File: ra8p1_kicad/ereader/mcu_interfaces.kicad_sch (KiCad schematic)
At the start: 3 parts, among them U1 R7KA8P1KFLCAC#UC0

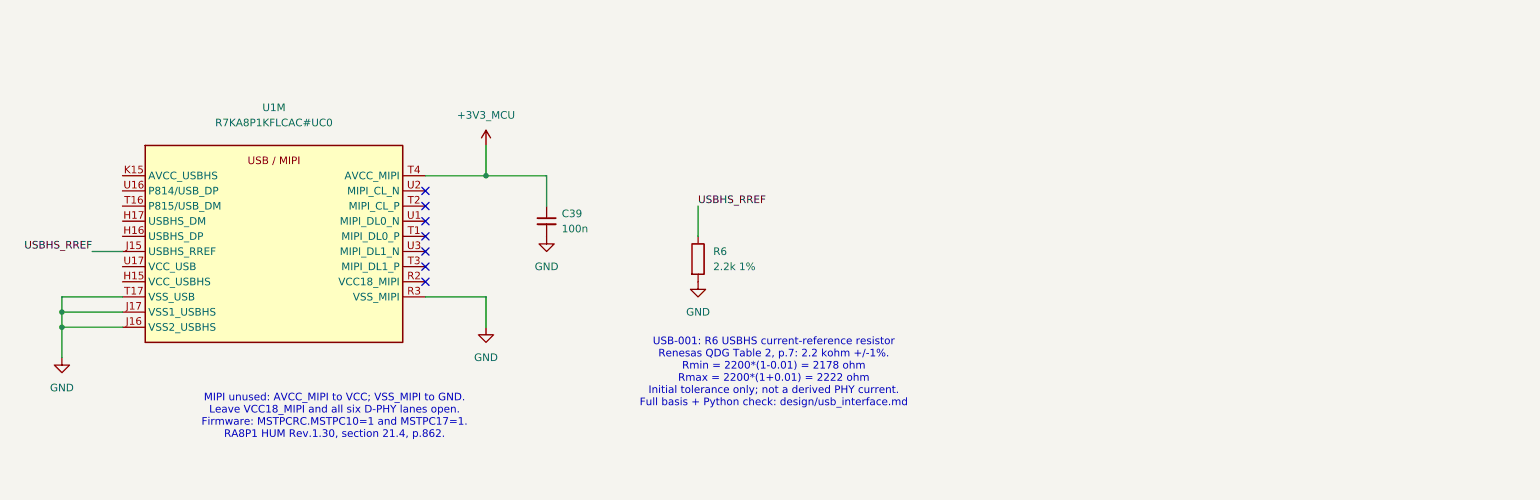
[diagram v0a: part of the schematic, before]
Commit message: feat(hardware): wire USB full-speed supply bypass
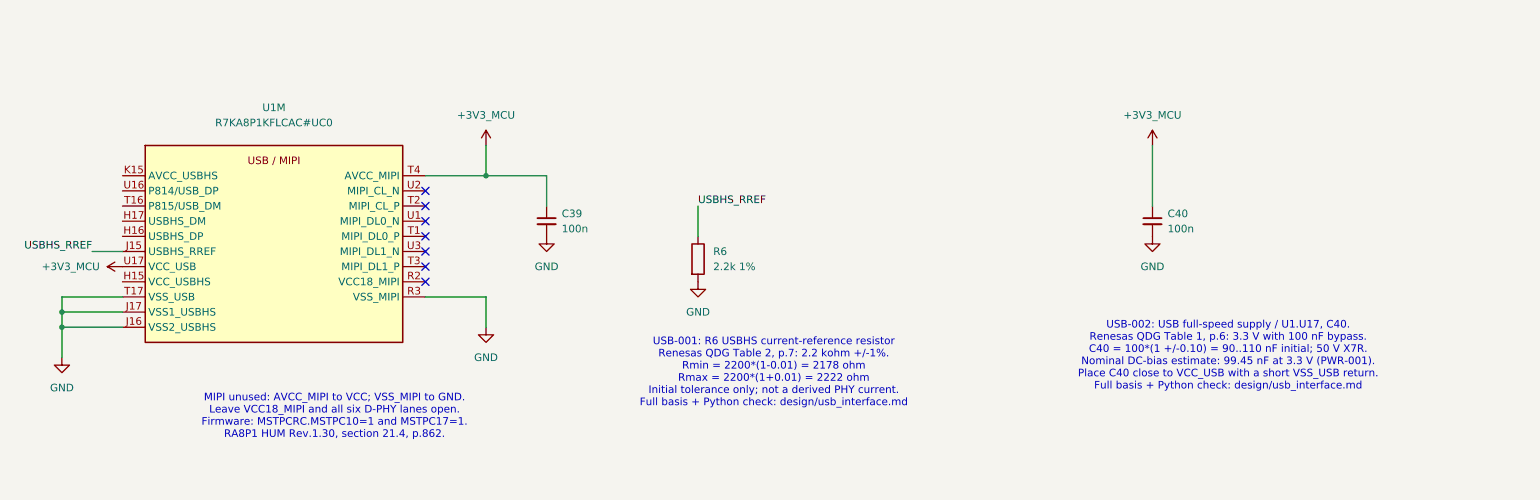
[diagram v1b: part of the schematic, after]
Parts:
- added C40: 100n, symbol Device:C_Small
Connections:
- net +3V3_MCU: now also U1.U17 (VCC_USB), C40.1
- net GND: now also C40.2
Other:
- note added: "USB-002: USB full-speed supply / U1.U17, C40. Renesas QDG Table 1, p.6: 3.3 V with 100 nF bypass. C40 = 100*(1 +/-0.10) = 90..110 nF initial; 50 V X7R. Nominal DC-bias estimate: 99.45 nF at 3.3 V (PWR-001). Place C40 close to VCC_USB with a short VSS_USB return. Full basis + Python check: design/usb_interface.md"

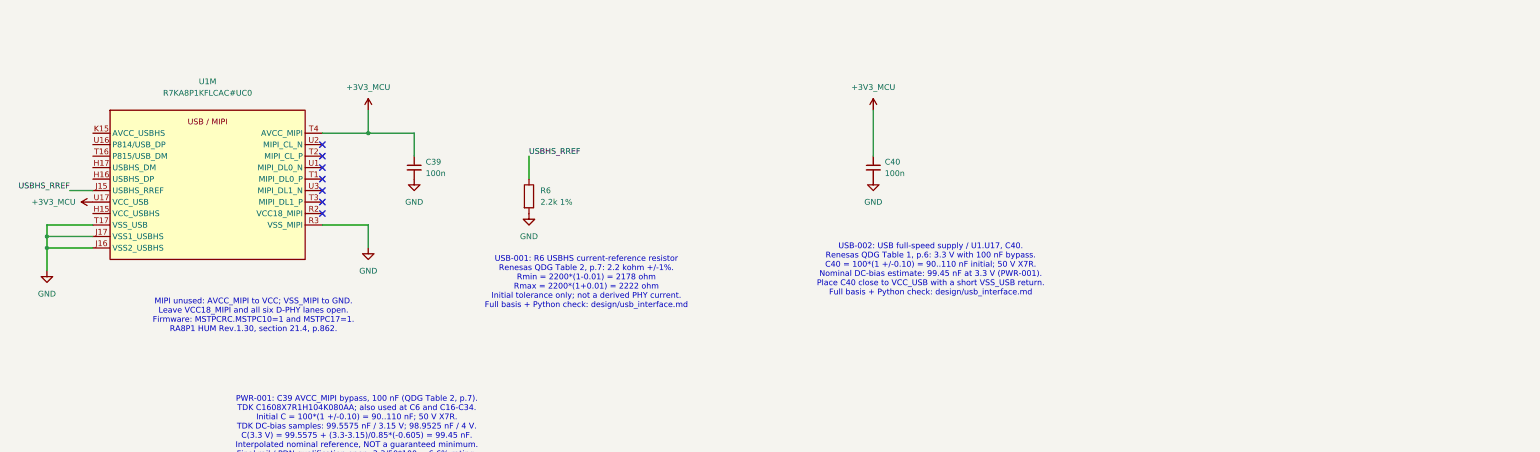
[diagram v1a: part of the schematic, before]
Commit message: feat(hardware): wire USB high-speed supply bypass and bulk
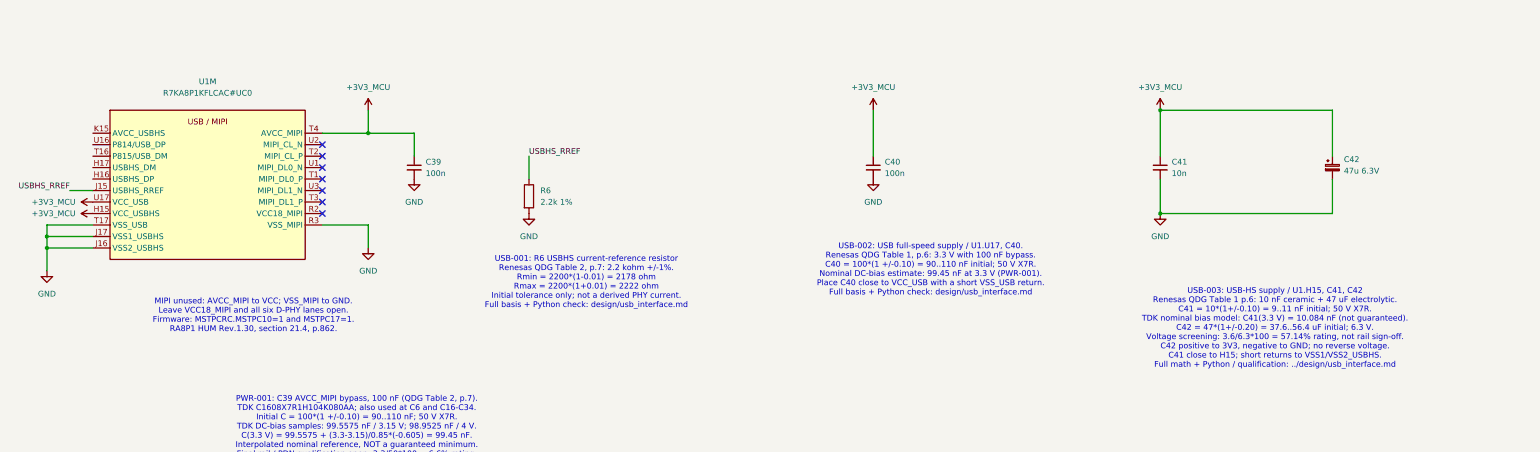
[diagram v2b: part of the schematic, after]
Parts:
- added C41: 10n, symbol Device:C_Small
- added C42: 47u 6.3V, symbol Device:C_Polarized_Small
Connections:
- net +3V3_MCU: now also U1.H15 (VCC_USBHS), C41.1, C42.1
- net GND: now also C41.2, C42.2
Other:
- note added: "USB-003: USB-HS supply / U1.H15, C41, C42 Renesas QDG Table 1 p.6: 10 nF ceramic + 47 uF electrolytic. C41 = 10*(1+/-0.10) = 9..11 nF initial; 50 V X7R. TDK nominal bias model: C41(3.3 V) = 10.084 nF (not guaranteed). C42 = 47*(1+/-0.20) = 37.6..56.4 uF initial; 6.3 V. Voltage screening: 3.6/6.3*100 = 57.14% rating, not rail sign-off. C42 positive to 3V3, negative to GND; no reverse voltage. C41 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"

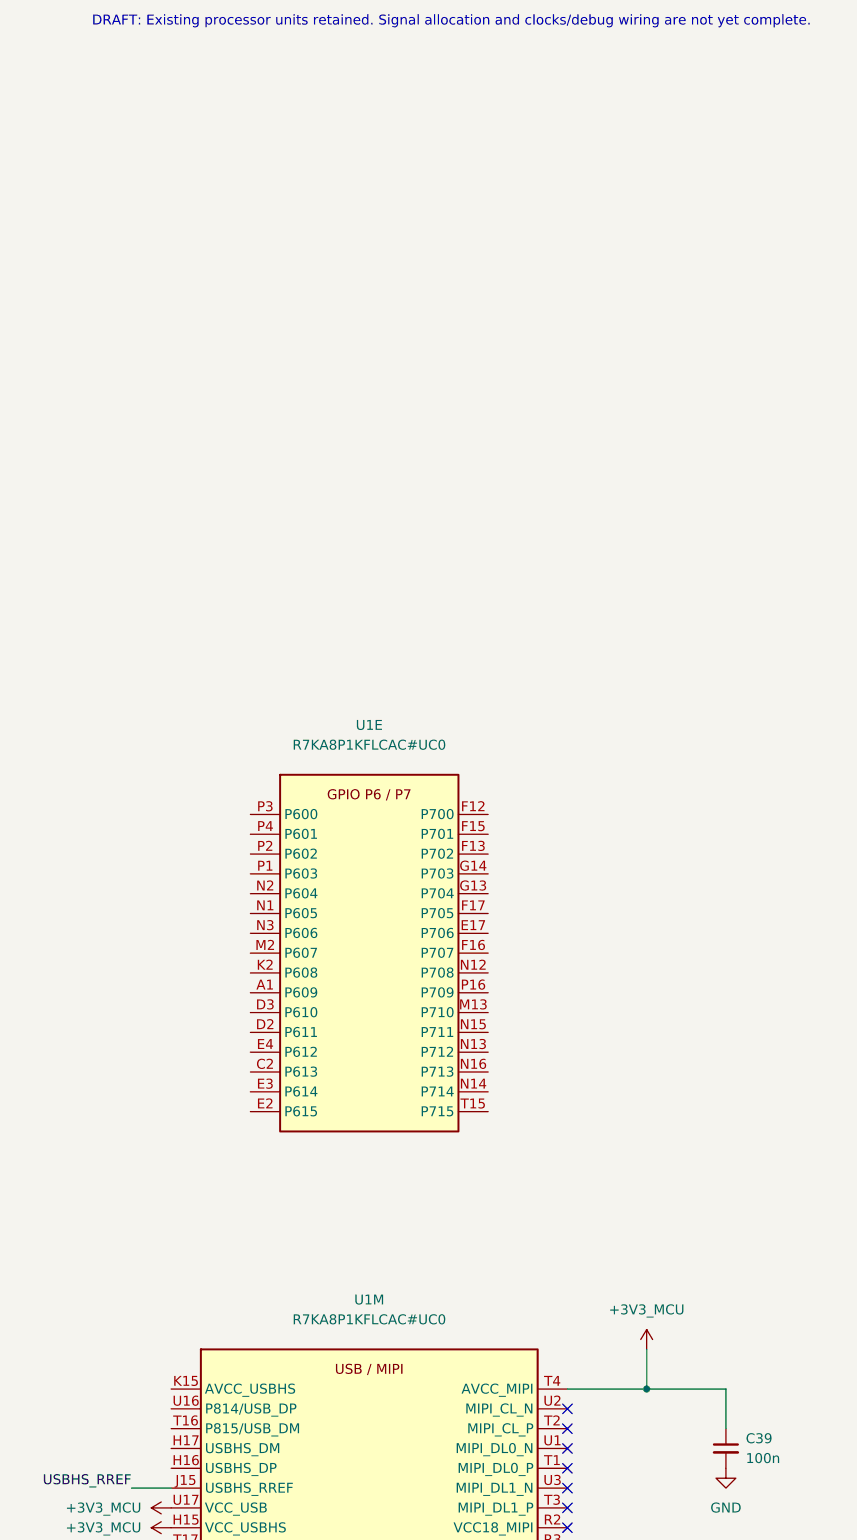
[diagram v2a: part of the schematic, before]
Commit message: feat(hardware): add USB high-speed analog supply filter
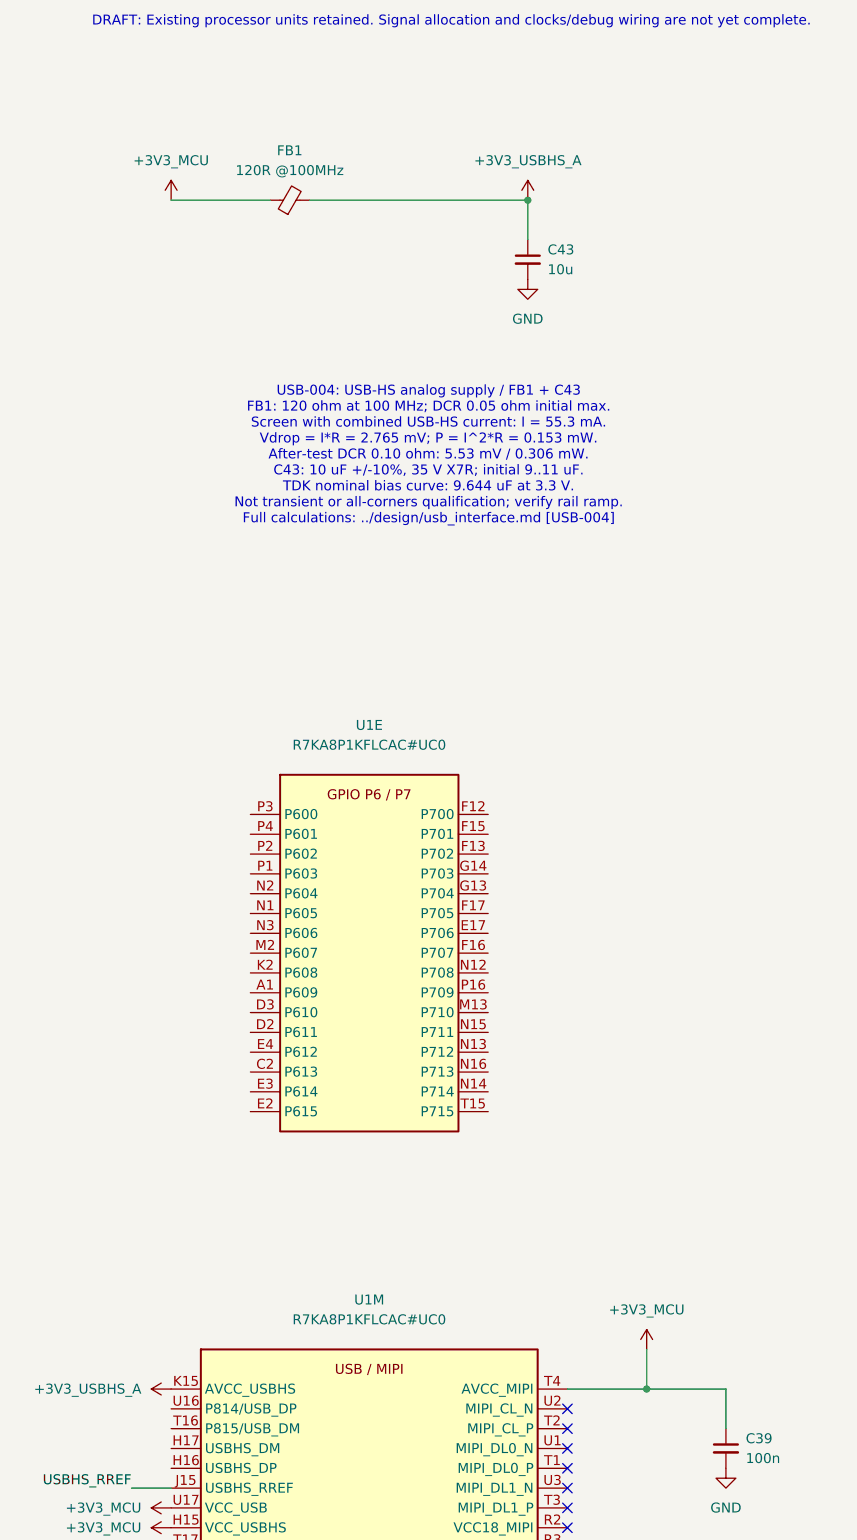
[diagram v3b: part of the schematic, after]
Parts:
- added C43: 10u, symbol Device:C_Small
- added FB1: 120R @100MHz, symbol Device:FerriteBead_Small
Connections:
- net +3V3_MCU: now also FB1.1
- net GND: now also C43.2
- net +3V3_USBHS_A: now reaches U1.K15 (AVCC_USBHS)
- net +3V3_USBHS_A: now also C43.1, FB1.2
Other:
- note added: "USB-004: USB-HS analog supply / FB1 + C43 FB1: 120 ohm at 100 MHz; DCR 0.05 ohm initial max. Screen with combined USB-HS current: I = 55.3 mA. Vdrop = I*R = 2.765 mV; P = I^2*R = 0.153 mW. After-test DCR 0.10 ohm: 5.53 mV / 0.306 mW. C43: 10 uF +/-10%, 35 V X7R; initial 9..11 uF. TDK nominal bias curve: 9.644 uF at 3.3 V. Not transient or all-corners qualification; verify rail ramp. Full calculat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"

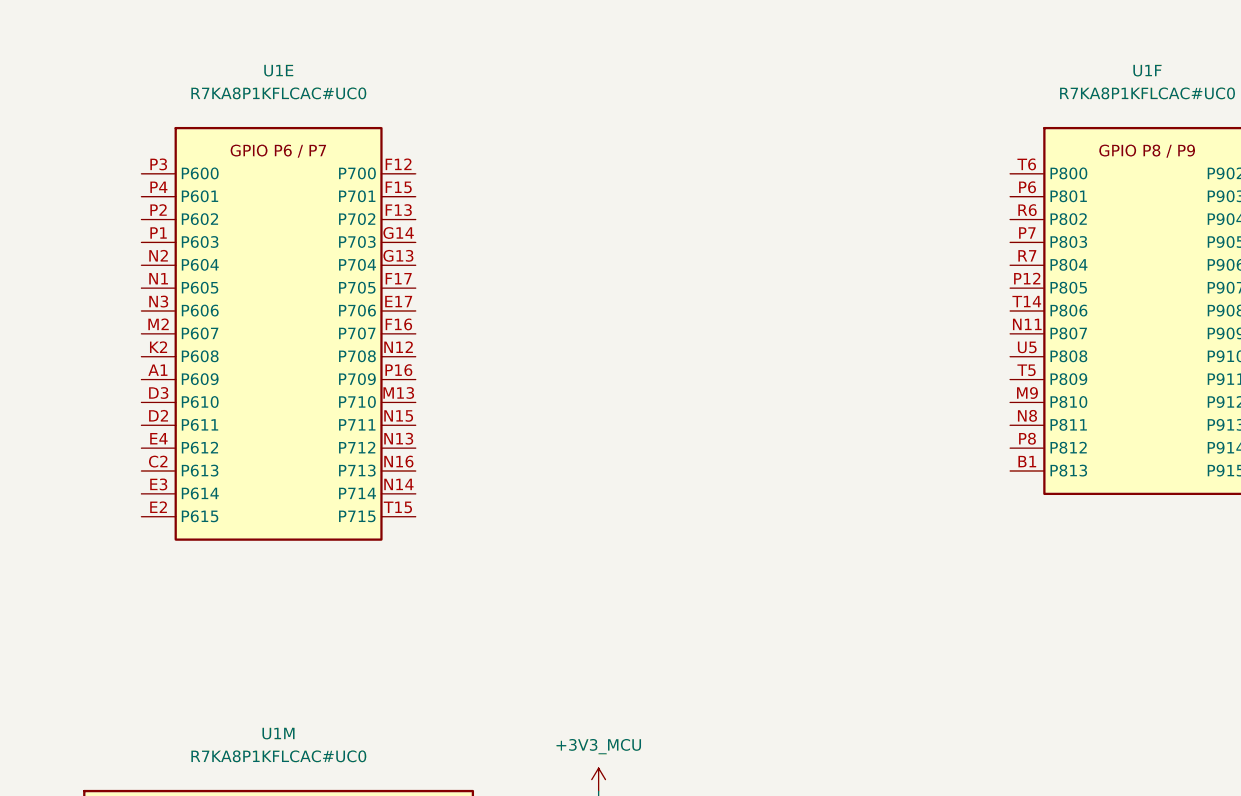
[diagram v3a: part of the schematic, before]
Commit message: Allocate RA8P1 SPI radio interface and connect power enable
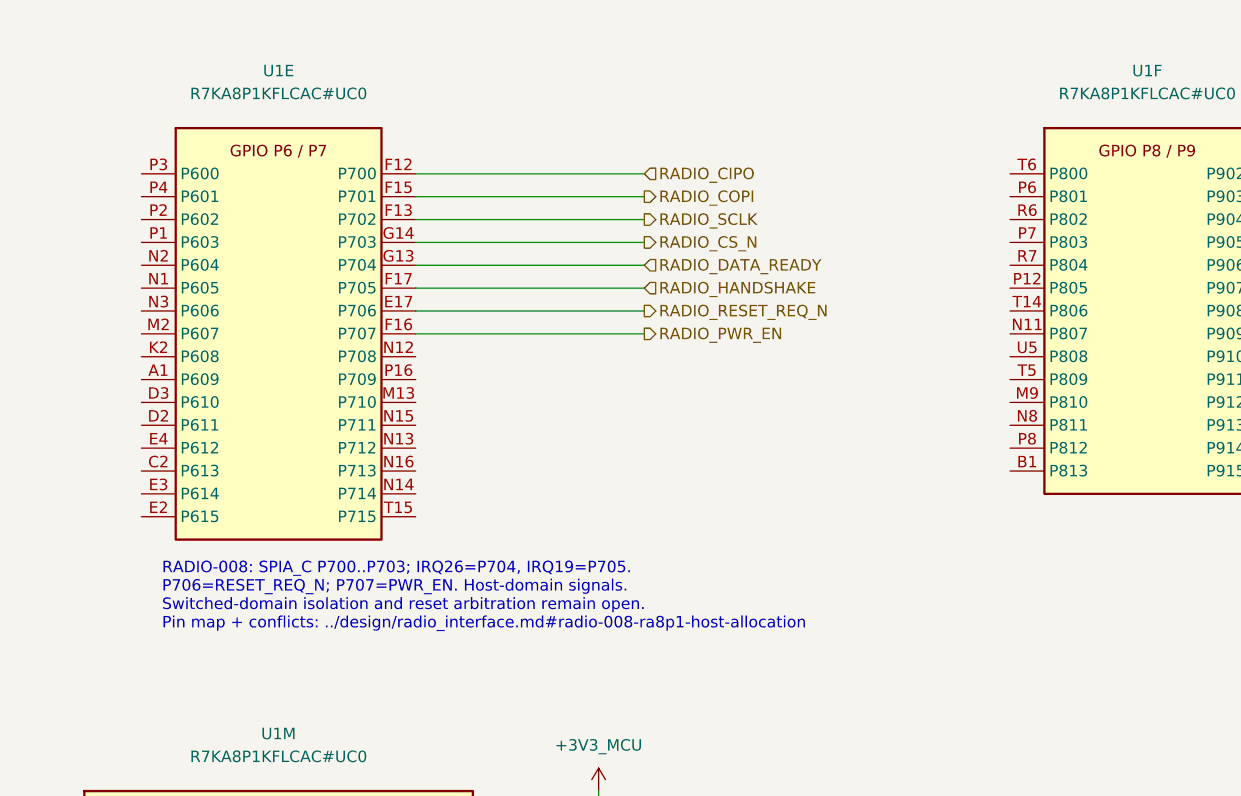
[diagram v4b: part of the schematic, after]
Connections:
- net RADIO_RESET_REQ_N: now reaches U1.E17 (P706)
- net RADIO_CIPO: now reaches U1.F12 (P700)
- net RADIO_SCLK: now reaches U1.F13 (P702)
- net RADIO_COPI: now reaches U1.F15 (P701)
- net RADIO_PWR_EN: now reaches U1.F16 (P707)
- net RADIO_HANDSHAKE: now reaches U1.F17 (P705)
- net RADIO_DATA_READY: now reaches U1.G13 (P704)
- net RADIO_CS_N: now reaches U1.G14 (P703)
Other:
- note added: "RADIO-008: SPIA_C P700..P703; IRQ26=P704, IRQ19=P705. P706=RESET_REQ_N; P707=PWR_EN. Host-domain signals. Switched-domain isolation and reset arbitration remain open. Pin map + conflicts: ../design/radio_interface.md#radio-008-ra8p1-host-allocation"
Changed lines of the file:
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@@
+		)
+	)
+	(text "RADIO-008: SPIA_C P700..P703; IRQ26=P704, IRQ19=P705.\nP706=RESET_REQ_N; P707=PWR_EN. Host-domain signals.\nSwitched-domain isolation and reset arbitration remain open.\nPin map + conflicts: ../design/radio_interface.md#radio-008-ra8p1-host-allocation"
+		(exclude_from_sim no)
+		(at 42.926 165.1 0)
+		(effects
+			(font
+				(size 1.27 1.27)
+			)
+			(justify left top)
+			(href "https://github.com/bsikar/ra8-firmware/blob/design/ereader-circuit/ra8p1_kicad/design/radio_interface.md#radio-008-ra8p1-host-allocation")
 		)
 	)
@@
 	(wire
 		(pts
+			(xy 71.12 124.46) (xy 96.52 124.46)
+		)
+		(stroke
+			(width 0)
+			(type default)
+		)
+	)
+	(wire
+		(pts
 			(xy 76.2 48.26) (xy 76.2 43.18)
 		)
@@
 	(wire
 		(pts
+			(xy 71.12 134.62) (xy 96.52 134.62)
+		)
+		(stroke
+			(width 0)
+			(type default)
+		)
+	)
+	(wire
+		(pts
+			(xy 71.12 137.16) (xy 96.52 137.16)
+		)
+		(stroke
+			(width 0)
+			(type default)
+		)
+	)
+	(wire
+		(pts
+			(xy 71.12 132.08) (xy 96.52 132.08)
+		)
+		(stroke
+			(width 0)
+			(type default)
+		)
+	)
+	(wire
+		(pts
+			(xy 71.12 129.54) (xy 96.52 129.54)
+		)
+		(stroke
+			(width 0)
+			(type default)
+		)
+	)
+	(wire
+		(pts
 			(xy 25.4 208.28) (xy 30.48 208.28)
 		)
@@
 	(wire
 		(pts
+			(xy 71.12 127) (xy 96.52 127)
+		)
+		(stroke
+			(width 0)
+			(type default)
+		)
+	)
+	(wire
+		(pts
 			(xy 304.8 205.74) (xy 304.8 213.36)
 		)
@@
 	(wire
 		(pts
+			(xy 71.12 121.92) (xy 96.52 121.92)
+		)
+		(stroke
+			(width 0)
+			(type default)
+		)
+	)
+	(wire
+		(pts
 			(xy 48.26 43.18) (xy 76.2 43.18)
+		)
+		(stroke
+			(width 0)
+			(type default)
+		)
+	)
+	(wire
+		(pts
+			(xy 71.12 139.7) (xy 96.52 139.7)
 		)
 		(stroke
@@
 		)
 	)
+	(hierarchical_label "RADIO_DATA_READY"
+		(shape input)
+		(at 96.52 132.08 0)
+		(effects
+			(font
+				(size 1.27 1.27)
+			)
+			(justify left)
+		)
+	)
+	(hierarchical_label "RADIO_SCLK"
+		(shape output)
+		(at 96.52 127 0)
+		(effects
+			(font
+				(size 1.27 1.27)
+			)
+			(justify left)
+		)
+	)
+	(hierarchical_label "RADIO_PWR_EN"
+		(shape output)
+		(at 96.52 139.7 0)
+		(effects
+			(font
+				(size 1.27 1.27)
+			)
+			(justify left)
+		)
+	)
+	(hierarchical_label "RADIO_CIPO"
+		(shape input)
+		(at 96.52 121.92 0)
+		(effects
+			(font
+				(size 1.27 1.27)
+			)
+			(justify left)
+		)
+	)
+	(hierarchical_label "RADIO_COPI"
+		(shape output)
+		(at 96.52 124.46 0)
+		(effects
+			(font
+				(size 1.27 1.27)
+			)
+			(justify left)
+		)
+	)
+	(hierarchical_label "RADIO_CS_N"
+		(shape output)
+		(at 96.52 129.54 0)
+		(effects
+			(font
+				(size 1.27 1.27)
+			)
+			(justify left)
+		)
+	)
+	(hierarchical_label "RADIO_HANDSHAKE"
+		(shape input)
+		(at 96.52 134.62 0)
+		(effects
+			(font
+				(size 1.27 1.27)
+			)
+			(justify left)
+		)
+	)
+	(hierarchical_label "RADIO_RESET_REQ_N"
+		(shape output)
+		(at 96.52 137.16 0)
+		(effects
+			(font
+				(size 1.27 1.27)
+			)
+			(justify left)
+		)
+	)
